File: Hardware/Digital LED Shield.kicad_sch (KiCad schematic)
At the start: 13 parts, among them J1 Conn_02x10_Odd_Even, J2 Conn_01x03_Male, J3 Barrel_Jack_MountingPin, J4 Conn_01x02_Female, U1 SN74LVC1T45DBV

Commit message: add protection
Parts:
- added D2: LM66100DCKR, SOP65P210X110-6N, symbol LM66100DCKR:LM66100DCKR
- added IC1: LM431BCM3X_NOPB, LM431BCM3X:SOT95P237X95-3N, symbol LM431BCM3X_NOPB:LM431BCM3X_NOPB
- added IC2: LM66200DRLR, SOTFL50P160X60-8N, symbol LM66200DRLR:LM66200DRLR
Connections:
- net +5VP: now also D2.6 (VOUT); no longer JP2.2 (B)
- net GND: now also IC2.1 (GND_1), IC2.4 (~{ON}), IC2.5 (GND_2)
- new net +5VD: D2.1 (VIN), JP2.2 (B)
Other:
- note added: "Pi Connector"
- note added: "Power"
- note added: "Protection"
- moved on the sheet: C1, C2, C3, C4, D1, J1, J2, J3, J4, JP1, JP2, R1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

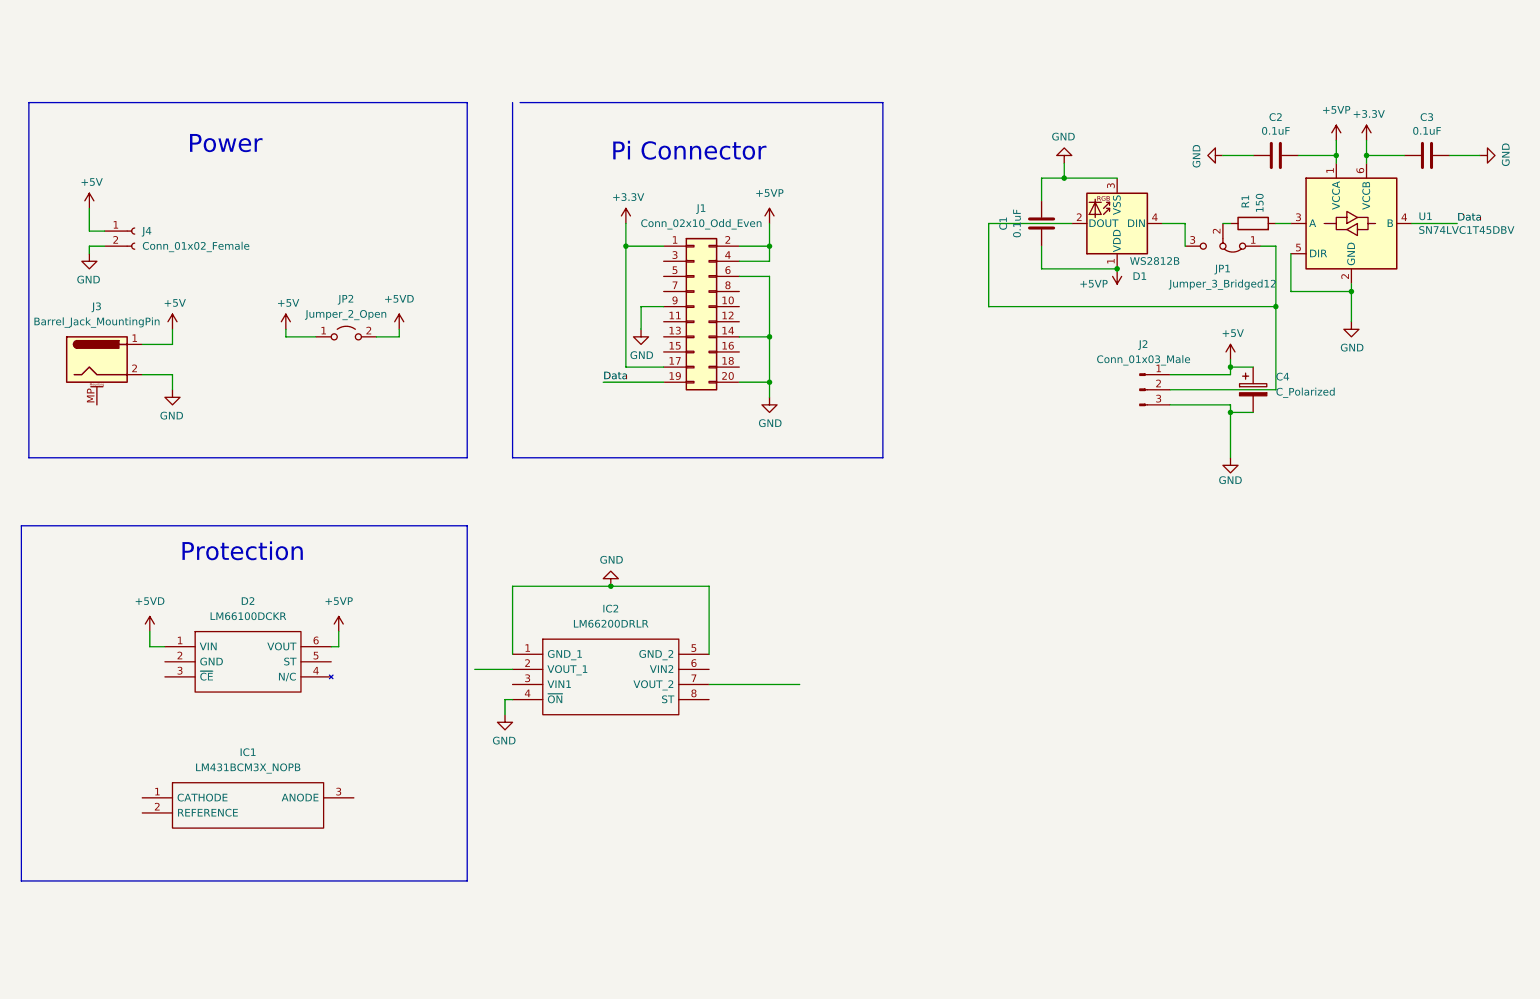
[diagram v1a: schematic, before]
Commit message: Add protection and screw terminal
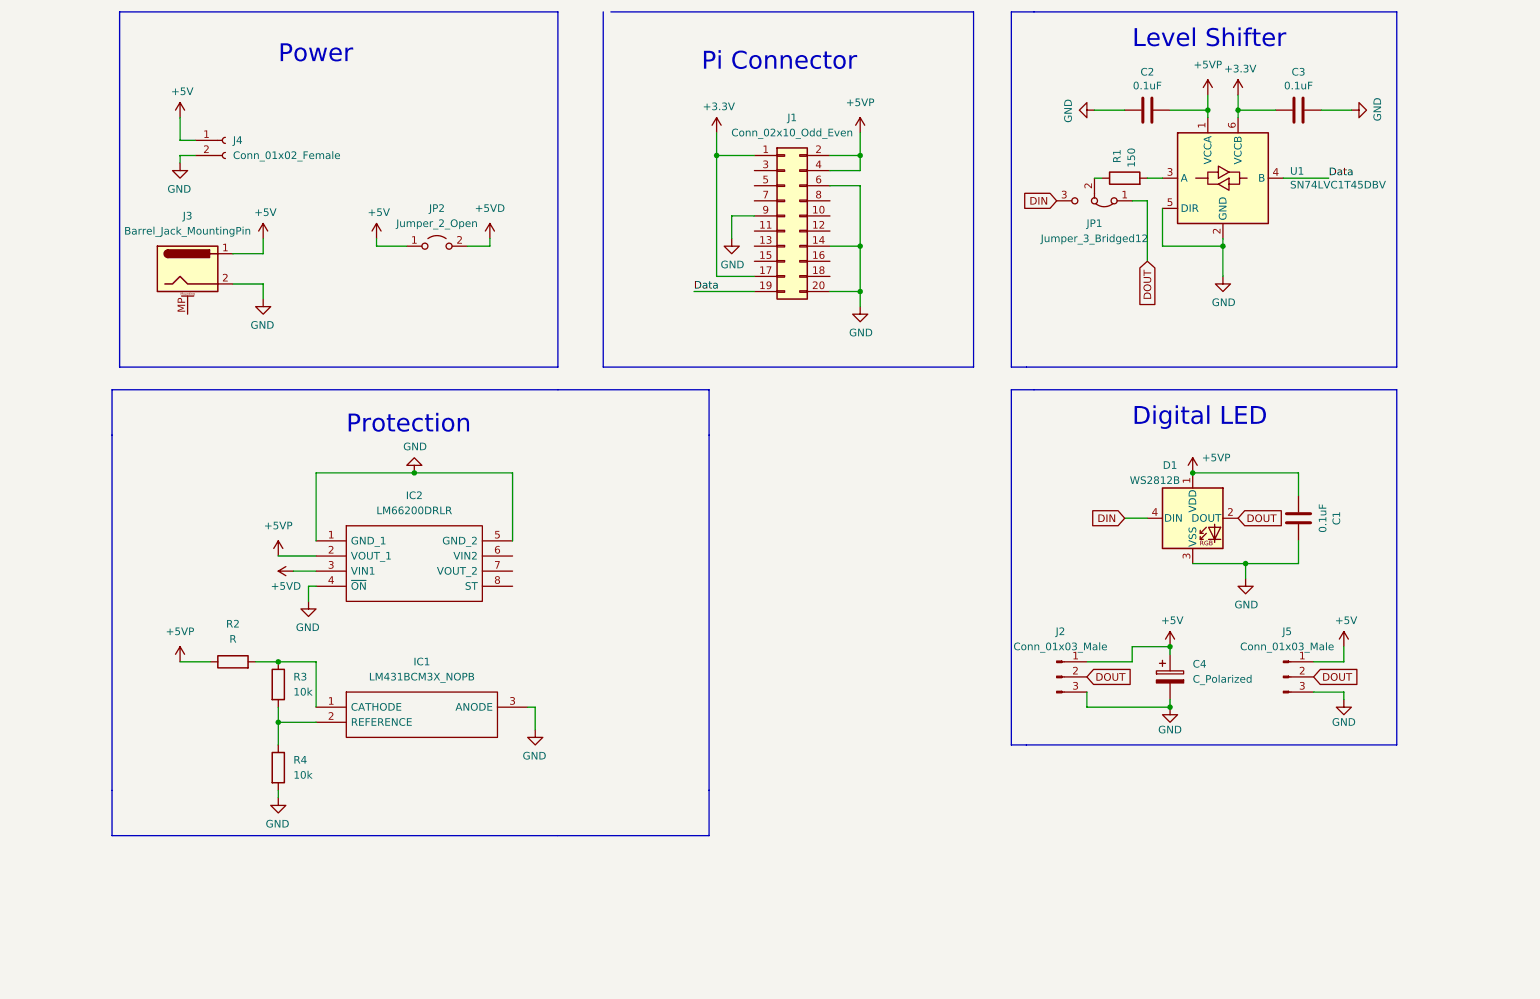
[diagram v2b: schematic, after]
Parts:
- removed D2: LM66100DCKR, SOP65P210X110-6N, symbol LM66100DCKR:LM66100DCKR
- added J5: Conn_01x03_Male, Connector_JST:JST_EH_B3B-EH-A_1x03_P2.50mm_Vertical, symbol Connector:Conn_01x03_Male
- added R2: R, Resistor_SMD:R_0603_1608Metric, symbol Device:R
- added R3, R4: 10k, Resistor_SMD:R_0603_1608Metric, symbol Device:R
- IC2: footprint SOTFL50P160X60-8N -> LM66200DRLR:SOTFL50P160X60-8N
- J4: footprint Connector_PinHeader_2.54mm:PinHeader_1x02_P2.54mm_Vertical -> TerminalBlock_Phoenix:TerminalBlock_Phoenix_MKDS-1,5-2-5.08_1x02_P5.08mm_Horizontal
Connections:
- net +5V: now also J5.1 (Pin_1)
- net +5VD: now also IC2.3 (VIN1)
- net +5VP: now also IC2.2 (VOUT_1), R2.1
- net GND: now also IC1.3 (ANODE), J5.3 (Pin_3), R4.2
- net DOUT: now reaches D1.2 (DOUT), J2.2 (Pin_2), JP1.1 (A)
- net DOUT: now also J5.2 (Pin_2)
- net DIN: now reaches D1.4 (DIN), JP1.3 (B)
- net at IC1.1 (CATHODE): now also R2.2, R3.1
- net at IC1.2 (REFERENCE): now also R3.2, R4.1
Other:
- note added: "Digital LED"
- note added: "Level Shifter"
- moved on the sheet: C1, C4, D1, IC1, IC2, J1, J2, J3, J4, JP2

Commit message: Add ordered Version V1
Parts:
- C4: value C_Polarized -> 10uF
- R2: value R -> 1k
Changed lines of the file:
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@@
     (in_bom yes) (on_board yes) (fields_autoplaced)
     (property "Reference" "R2" (id 0) (at 53.34 129.54 90))
-    (property "Value" "R" (id 1) (at 53.34 132.08 90))
+    (property "Value" "1k" (id 1) (at 53.34 132.08 90))
     (property "Footprint" "Resistor_SMD:R_0603_1608Metric" (id 2) (at 53.34 137.668 90)
       (effects (font (size 1.27 1.27)) hide)
@@
       (effects (font (size 1.27 1.27)) (justify left))
     )
-    (property "Value" "C_Polarized" (id 1) (at 214.63 138.8109 0)
+    (property "Value" "10uF" (id 1) (at 214.63 138.8109 0)
       (effects (font (size 1.27 1.27)) (justify left))
     )
@@
     )
     (path "/a3108c40-70ec-47c8-a063-e90dda858ab8"
-      (reference "C4") (unit 1) (value "C_Polarized") (footprint "Capacitor_THT:CP_Radial_D4.0mm_P1.50mm")
+      (reference "C4") (unit 1) (value "10uF") (footprint "Capacitor_THT:CP_Radial_D4.0mm_P1.50mm")
     )
     (path "/73e6ff64-8915-4bf2-8341-ad1e32b02655"
@@
     )
     (path "/893674fc-4f39-4e3b-8333-425fcaa60382"
-      (reference "R2") (unit 1) (value "R") (footprint "Resistor_SMD:R_0603_1608Metric")
+      (reference "R2") (unit 1) (value "1k") (footprint "Resistor_SMD:R_0603_1608Metric")
     )
     (path "/23b875db-d2ae-47f5-8c5a-f411ad1dfc31"

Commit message: change lm431 to TPS2420
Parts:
- removed IC1: LM431BCM3X_NOPB, LM431BCM3X:SOT95P237X95-3N, symbol LM431BCM3X_NOPB:LM431BCM3X_NOPB
- removed R2: 1k, Resistor_SMD:R_0603_1608Metric, symbol Device:R
- removed R3, R4: 10k, Resistor_SMD:R_0603_1608Metric, symbol Device:R
- added IC1: TPS2420RSAT, QFN65P400X400X100-17N, symbol TPS2420RSAT:TPS2420RSAT
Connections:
- net +3V3: no longer J1.1 (Pin_1)
- net +5VP: now also IC1.10 (VOUT_2), IC1.11 (VOUT_3); no longer IC2.2 (VOUT_1)
- net GND: now also IC1.5 (GND)
- new net +5VL: IC1.1 (VIN_2), IC1.2 (VIN_3), IC1.3 (VIN_4), IC1.4 (VIN), IC2.2 (VOUT_1)

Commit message: update sch and pcb
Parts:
- removed JP1: Jumper_3_Bridged12, Jumper:SolderJumper-3_P1.3mm_Bridged12_Pad1.0x1.5mm, symbol Jumper:Jumper_3_Bridged12
- added JP1: Jumper_3_Open, Jumper:SolderJumper-3_P1.3mm_Open_Pad1.0x1.5mm, symbol Jumper:Jumper_3_Open
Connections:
- net +5VD: now also IC1.1 (VIN_2), IC1.2 (VIN_3), IC1.3 (VIN_4), IC1.4 (VIN); no longer IC2.3 (VIN1)
- net +5VL: now also IC1.10 (VOUT_2), IC1.11 (VOUT_3), IC1.12 (VOUT), IC2.3 (VIN1); no longer IC1.1 (VIN_2), IC1.2 (VIN_3), IC1.3 (VIN_4), IC1.4 (VIN), IC2.2 (VOUT_1)
- net +5VP: now also IC2.2 (VOUT_1); no longer IC1.10 (VOUT_2), IC1.11 (VOUT_3)
- net DIN: now also JP1.3 (B)
- net DOUT: now also JP1.1 (A)
- net GND: now also IC1.16 (~{EN}), IC1.6 (LTCH), J3.MP (MountPin)
- net at R1.1: now also JP1.2 (C)

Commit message: add Gerber
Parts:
- added JP3: Jumper_2_Open, Jumper:SolderJumper-2_P1.3mm_Open_Pad1.0x1.5mm, symbol Jumper:Jumper_2_Open
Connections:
- net DOUT: now also JP3.2 (B); no longer D1.2 (DOUT)
- new net DOI: D1.2 (DOUT), JP3.1 (A)
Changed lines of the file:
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@@
   (junction (at 67.31 153.67) (diameter 0) (color 0 0 0 0)
   )
+  (junction (at 207.01 71.12) (diameter 0) (color 0 0 0 0)
+  )
   (junction (at 67.31 158.75) (diameter 0) (color 0 0 0 0)
   )
@@
     (stroke (width 0) (type default) (color 0 0 0 0))
   )
+  (wire (pts (xy 207.01 58.42) (xy 207.01 71.12))
+    (stroke (width 0) (type default) (color 0 0 0 0))
+  )
   (polyline (pts (xy 115.57 26.67) (xy 115.57 86.36))
     (stroke (width 0) (type default) (color 0 0 0 0))
@@
     (stroke (width 0) (type default) (color 0 0 0 0))
   )
-  (wire (pts (xy 207.01 58.42) (xy 207.01 68.58))
-    (stroke (width 0) (type default) (color 0 0 0 0))
-  )
   (wire (pts (xy 210.82 133.35) (xy 210.82 134.62))
     (stroke (width 0) (type default) (color 0 0 0 0))
@@
   )
   (polyline (pts (xy 187.96 26.67) (xy 248.92 26.67))
+    (stroke (width 0) (type default) (color 0 0 0 0))
+  )
+  (wire (pts (xy 203.2 71.12) (xy 207.01 71.12))
     (stroke (width 0) (type default) (color 0 0 0 0))
   )
@@
     (effects (font (size 1.27 1.27)) (justify left bottom))
   )
-  (global_label "DOUT" (shape input) (at 222.25 111.76 0) (fields_autoplaced)
+  (global_label "DOI" (shape input) (at 222.25 111.76 0) (fields_autoplaced)
     (effects (font (size 1.27 1.27)) (justify left))
-    (property "Intersheet References" "${INTERSHEET_REFS}" (id 0) (at 229.5617 111.8394 0)
+    (property "Intersheet References" "${INTERSHEET_REFS}" (id 0) (at 227.8683 111.6806 0)
       (effects (font (size 1.27 1.27)) (justify left) hide)
     )
@@
     )
   )
+  (global_label "DOI" (shape input) (at 207.01 81.28 180) (fields_autoplaced)
+    (effects (font (size 1.27 1.27)) (justify right))
+    (property "Intersheet References" "${INTERSHEET_REFS}" (id 0) (at 201.3917 81.3594 0)
+      (effects (font (size 1.27 1.27)) (justify right) hide)
+    )
+  )
   (global_label "DOUT" (shape input) (at 196.85 138.43 0) (fields_autoplaced)
     (effects (font (size 1.27 1.27)) (justify left))
@@
     )
   )
-  (global_label "DOUT" (shape input) (at 207.01 68.58 270) (fields_autoplaced)
+  (global_label "DOUT" (shape input) (at 203.2 71.12 180) (fields_autoplaced)
     (effects (font (size 1.27 1.27)) (justify right))
-    (property "Intersheet References" "${INTERSHEET_REFS}" (id 0) (at 206.9306 75.8917 90)
+    (property "Intersheet References" "${INTERSHEET_REFS}" (id 0) (at 195.8883 71.0406 0)
       (effects (font (size 1.27 1.27)) (justify right) hide)
     )
@@
     )
     (pin "1")
+  )
+  (symbol (lib_id "Jumper:Jumper_2_Open") (at 207.01 76.2 90) (unit 1)
+    (in_bom yes) (on_board yes) (fields_autoplaced)
+    (property "Reference" "JP3" (id 0) (at 208.153 75.3653 90)
+      (effects (font (size 1.27 1.27)) (justify right))
+    )
+    (property "Value" "Jumper_2_Open" (id 1) (at 208.153 77.9022 90)
+      (effects (font (size 1.27 1.27)) (justify right))
+    )
+    (property "Footprint" "Jumper:SolderJumper-2_P1.3mm_Open_Pad1.0x1.5mm" (id 2) (at 207.01 76.2 0)
+      (effects (font (size 1.27 1.27)) hide)
+    )
+    (property "Datasheet" "~" (id 3) (at 207.01 76.2 0)
+      (effects (font (size 1.27 1.27)) hide)
+    )
+    (pin "1")
+    (pin "2")
   )
   (symbol (lib_id "Device:R") (at 203.2 54.61 90) (unit 1)
@@
       (effects (font (size 1.27 1.27)) hide)
     )
-    (property "Value" "+5V" (id 1) (at 211.201 128.9558 0))
+    (property "Value" "" (id 1) (at 211.201 128.9558 0))
     (property "Footprint" "" (id 2) (at 210.82 133.35 0)
       (effects (font (size 1.27 1.27)) hide)
@@
       (reference "#PWR0103") (unit 1) (value "+5VP") (footprint "")
     )
-    (path "/4373d9c4-82aa-4cac-b73d-946ee27a0b2d"
+    (path "/4373d9c4-82aa-4cac-b73d-946ee27a0b2e"
       (reference "#PWR0104") (unit 1) (value "+5V") (footprint "")
     )
@@
       (reference "JP2") (unit 1) (value "Jumper_2_Open") (footprint "Jumper:SolderJumper-2_P1.3mm_Open_Pad1.0x1.5mm")
     )
+    (path "/2bf92235-c40b-4aeb-94ab-c477a2ecaf36"
+      (reference "JP3") (unit 1) (value "Jumper_2_Open") (footprint "Jumper:SolderJumper-2_P1.3mm_Open_Pad1.0x1.5mm")
+    )
     (path "/340a3c97-4720-46c0-af55-cba214657808"

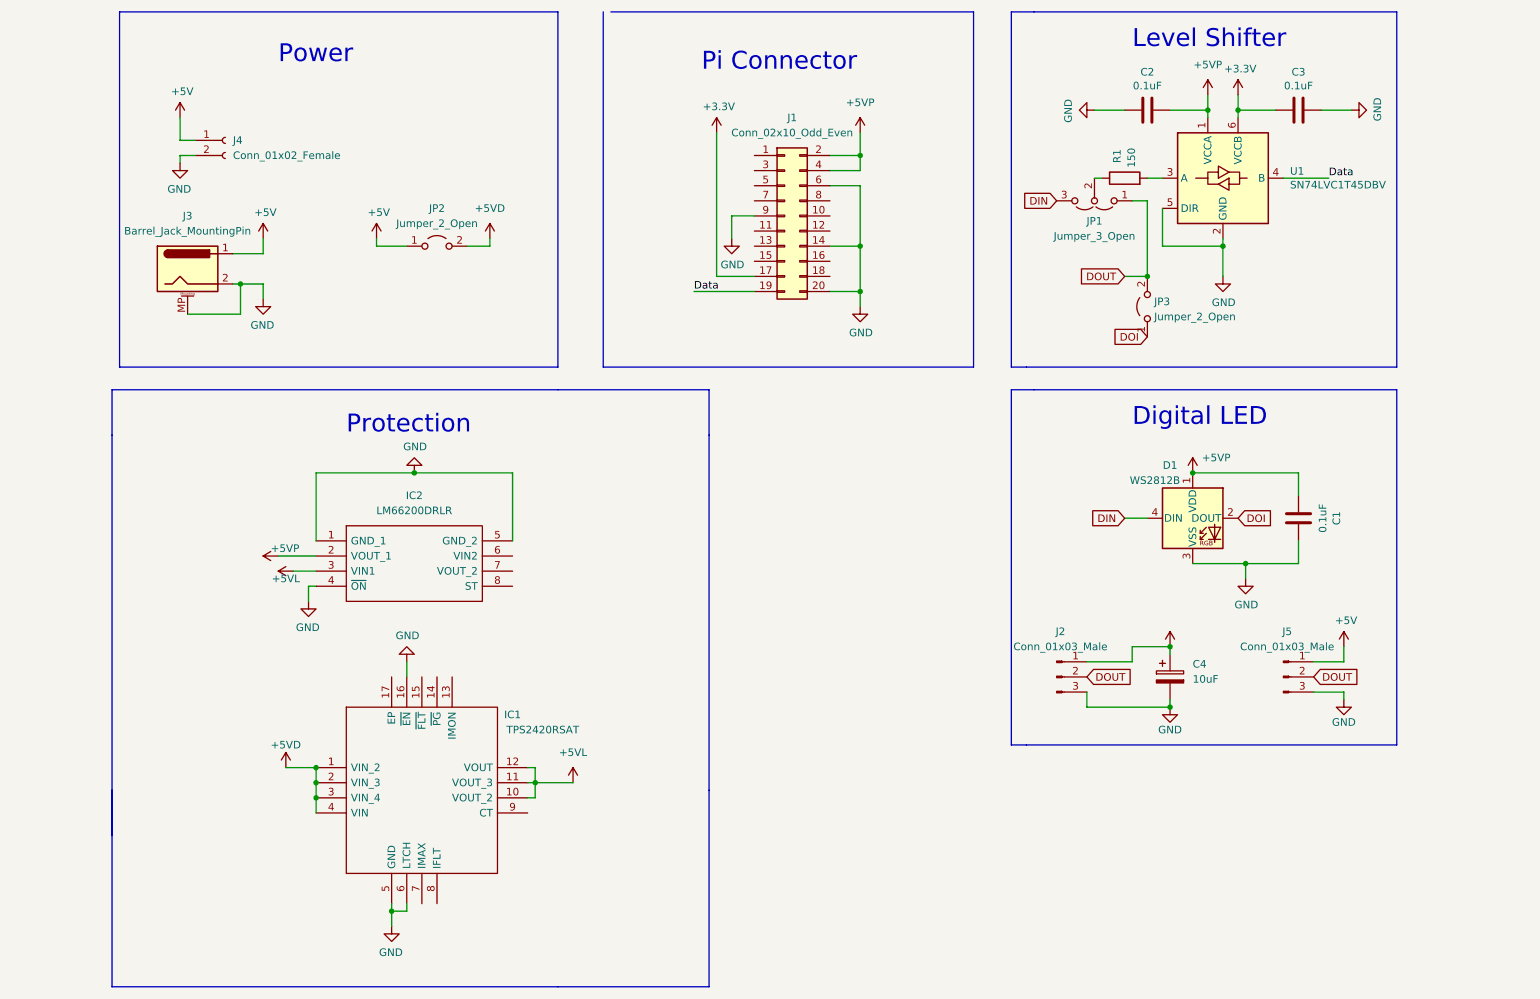
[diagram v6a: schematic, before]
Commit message: add eFuse for Overvoltage and Overcurrent protection
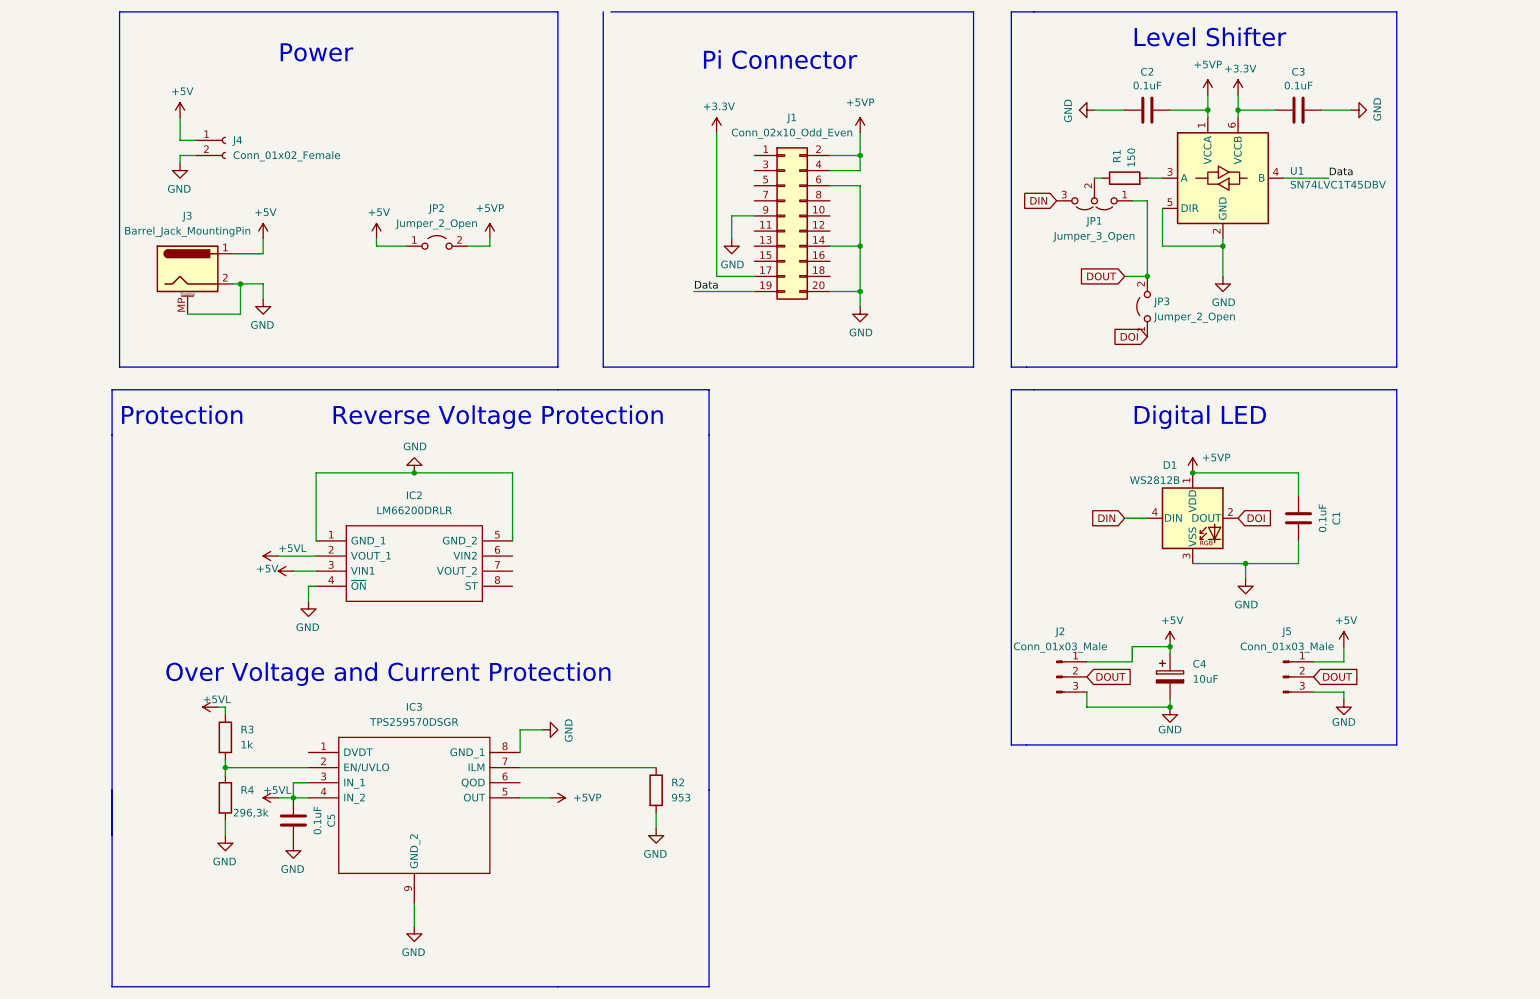
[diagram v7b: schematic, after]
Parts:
- removed IC1: TPS2420RSAT, QFN65P400X400X100-17N, symbol TPS2420RSAT:TPS2420RSAT
- added C5: 0.1uF, Capacitor_SMD:C_0603_1608Metric, symbol Device:C
- added IC3: TPS259570DSGR, TPS2595:SON50P200X200X80-9N, symbol TPS2595:TPS259570DSGR
- added R2: 953, Resistor_SMD:R_0603_1608Metric, symbol Device:R
- added R3: 1k, Resistor_SMD:R_0603_1608Metric, symbol Device:R
- added R4: 296,3k, Resistor_SMD:R_0603_1608Metric, symbol Device:R
- R1: footprint Resistor_SMD:R_0805_2012Metric -> Resistor_SMD:R_0603_1608Metric
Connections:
- net +5VD is gone; now on net +5VP: JP2.2 (B)
- net +5V: now also IC2.3 (VIN1)
- net +5VL: now also IC2.2 (VOUT_1), C5.2, IC3.3 (IN_1), IC3.4 (IN_2), R3.1; no longer IC2.3 (VIN1)
- net +5VP: now also IC3.5 (OUT); no longer IC2.2 (VOUT_1)
- net GND: now also C5.1, IC3.8 (GND_1), IC3.9 (GND_2), R2.2, R4.2
- new net: IC3.7 (ILM), R2.1
- new net: IC3.2 (EN/UVLO), R3.2, R4.1
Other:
- note added: "Over Voltage and Current Protection"
- note added: "Reverse Voltage Protection"
